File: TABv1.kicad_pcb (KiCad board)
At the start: 4 copper layers, 90 x 45 mm, 120 parts, among them IC1 TPS630702RNMR, J10 Conn_02x03_Odd_Even, J11 Conn_01x06_Pin, J5 Conn_02x08_Odd_Even, J6 Conn_02x08_Odd_Even, J7 503398-1892, J8 1053141104, J9 Conn_02x03_Odd_Even, Q1 MJD44H11T4G, Q10 PJM09P30DF, Q11 PJM09P30DF, Q12 PJM09P30DF, Q2 DMN2040U, Q3 DMN2040U, Q4 BC817-25,215, Q5 DMN2040U, Q6 DMN2040U, Q7 DMN2040U, SW1 BOOTSEL, SW2 RESET, U1 RP2350B-QFN80, U11 LPS22DF, U2 W25Q128JVS, U4 LSM6DSV80XTR, U5 LSM6DSV80XTR, U7 LM334M, U8 LIS2MDL, Y1 12MHz

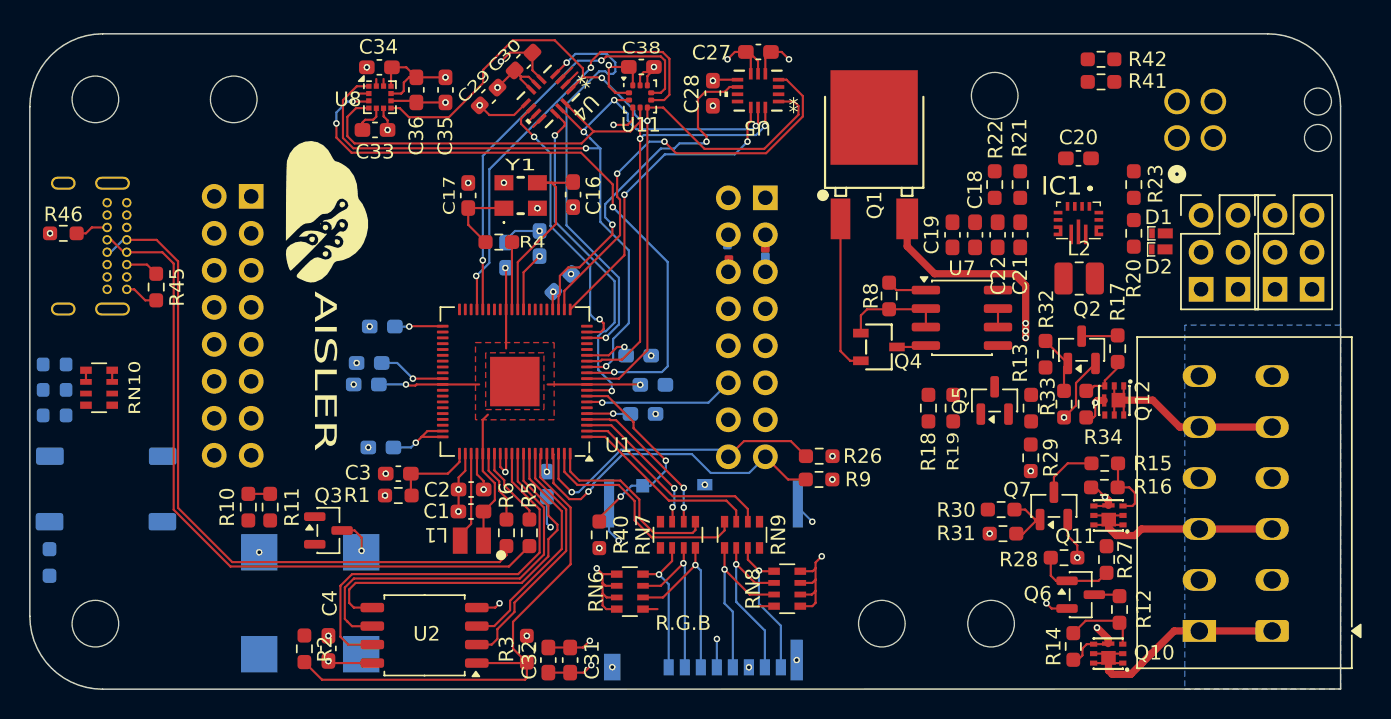
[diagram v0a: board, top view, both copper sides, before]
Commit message: nuovo routing completato (piste 0.15mm)
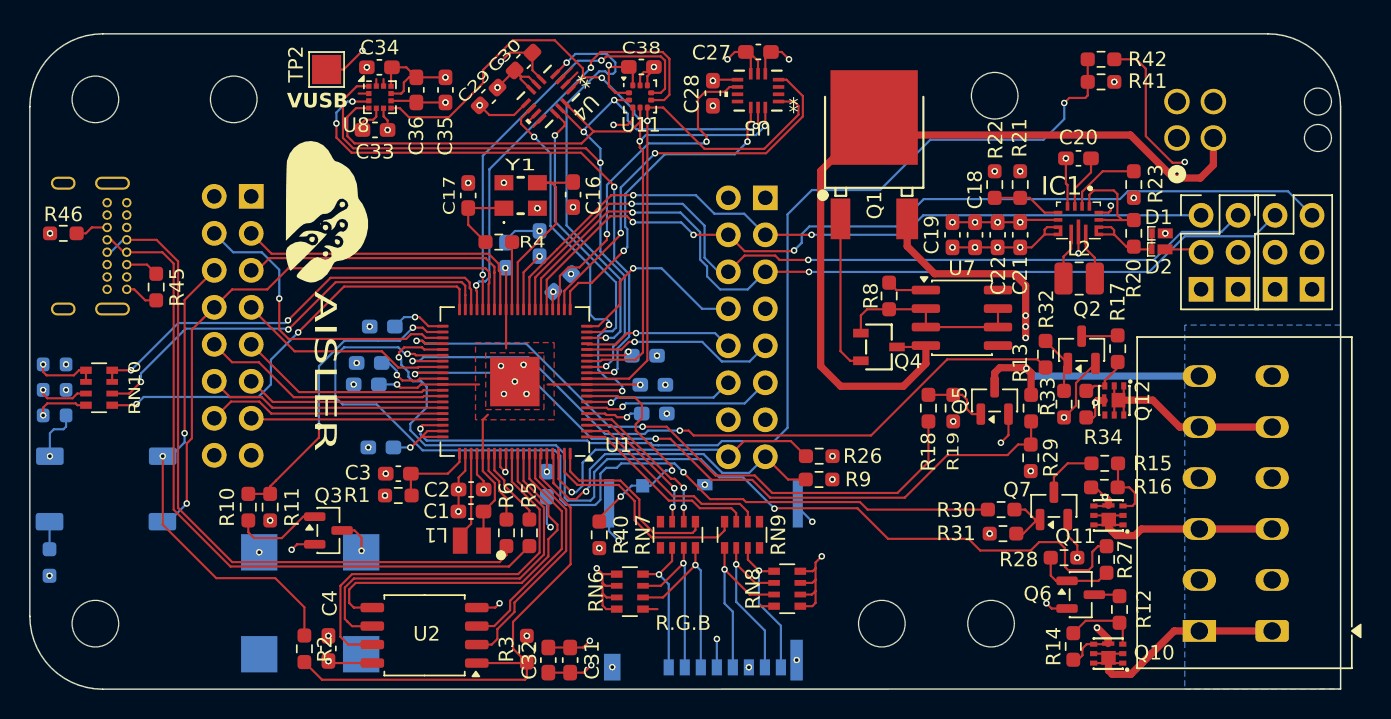
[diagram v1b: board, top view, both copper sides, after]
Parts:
- added TP2: TestPoint, TestPoint:TestPoint_Pad_2.0x2.0mm, F.Cu at (92.9, 36.0)
- moved C5 0.78 mm to (115.4, 59.6)
- moved C12 0.40 mm to (114.7, 55.6)
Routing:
- net /BATT_SENSE: track 0.00 -> 69.9 mm, vias 0 -> 2
- net /PYRO_FIRE_1: track 0.00 -> 69.6 mm, vias 0 -> 2
- net +BATT: track 2.02 -> 70.6 mm, vias 0 -> 1
- net /PYRO_FIRE_2: track 0.00 -> 63.9 mm, vias 0 -> 2
- net /PWM2: track 0.00 -> 60.3 mm, vias 0 -> 2
- net /PWM1: track 0.00 -> 60.2 mm, vias 0 -> 3
- net /PWM3: track 0.00 -> 57.6 mm, vias 0 -> 2
- net /PWM4: track 0.00 -> 52.4 mm, vias 0 -> 2
- net /PYRO_SENSE: track 0.00 -> 50.9 mm, vias 0 -> 2
- net /PYRO_FIRE_3: track 0.00 -> 50.5 mm, vias 0 -> 2
- net /PYRO_ENABLE: track 0.00 -> 45.0 mm, vias 0 -> 2
- net /RESET: track 0.00 -> 39.1 mm, vias 0 -> 1
- net BOOTSEL: track 0.00 -> 33.3 mm, vias 0 -> 2
- net /L_BLUE: track 0.00 -> 29.7 mm, vias 0 -> 2
- net /L_GREEN: track 0.00 -> 29.5 mm, vias 0 -> 2
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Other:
- board text added: "VUSB"

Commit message: USB impeadance matching, silkscreen fix, and routing improvement
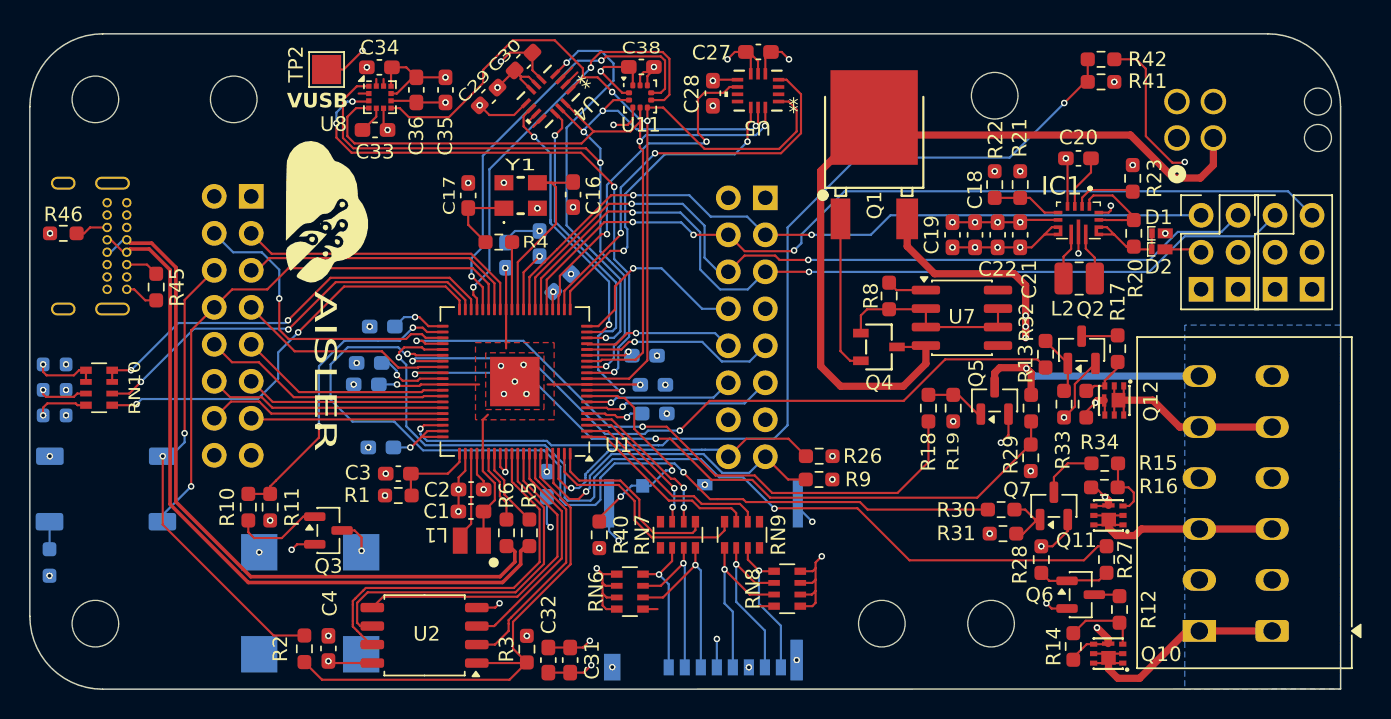
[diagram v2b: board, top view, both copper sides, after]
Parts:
- moved R28 1.57 mm to (141.9, 69.6), turned to -90 degrees
- moved R23 0.43 mm to (148.2, 43.4), turned to -90 degrees
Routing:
- net /PYRO_FIRE_1: track 69.6 -> 65.3 mm
- net GND: track 72.1 -> 68.6 mm, vias 62 -> 63
- net /SD0: track 25.5 -> 22.2 mm
- net /SD3: track 28.1 -> 25.8 mm
- net /BATT_SENSE: track 69.9 -> 68.0 mm
- net /SCLK: track 26.5 -> 24.8 mm
- net D-: track 47.7 -> 49.2 mm
- net D+: track 48.8 -> 50.1 mm
- net BOOTSEL: track 33.3 -> 32.1 mm
- net /L_GREEN: track 29.5 -> 28.6 mm
- net /IMU45_INT1: track 29.6 -> 28.8 mm
- net PG: track 5.13 -> 4.34 mm
- net /SD_detect: track 16.4 -> 15.6 mm
- net /RESET: track 39.1 -> 38.3 mm
- net /SCL_RADIO: track 22.3 -> 21.6 mm
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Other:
- board text removed: "R.G.B"

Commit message: fine rev 2.2
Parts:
- moved H6 2.50 mm to (84.0, 38.0)
- moved H1 0.79 mm to (138.0, 38.0)
- moved H4 0.50 mm to (138.0, 74.0)
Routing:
- net +BATT: track 70.6 -> 71.6 mm
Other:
- board text added: "+"
- board text added: "-"
- board text added: "PPS"
- board text added: "REV 2.2"
- board text added: "RST"
- board text removed: "REV 2.0"

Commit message: Ordine 1 Aprile
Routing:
- net GND: vias 63 -> 104
- added copper zone on B.Cu, net GND
- added copper zone on F.Cu, net GND
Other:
- board text added: "REV 2.3"
- board text removed: "REV 2.2"

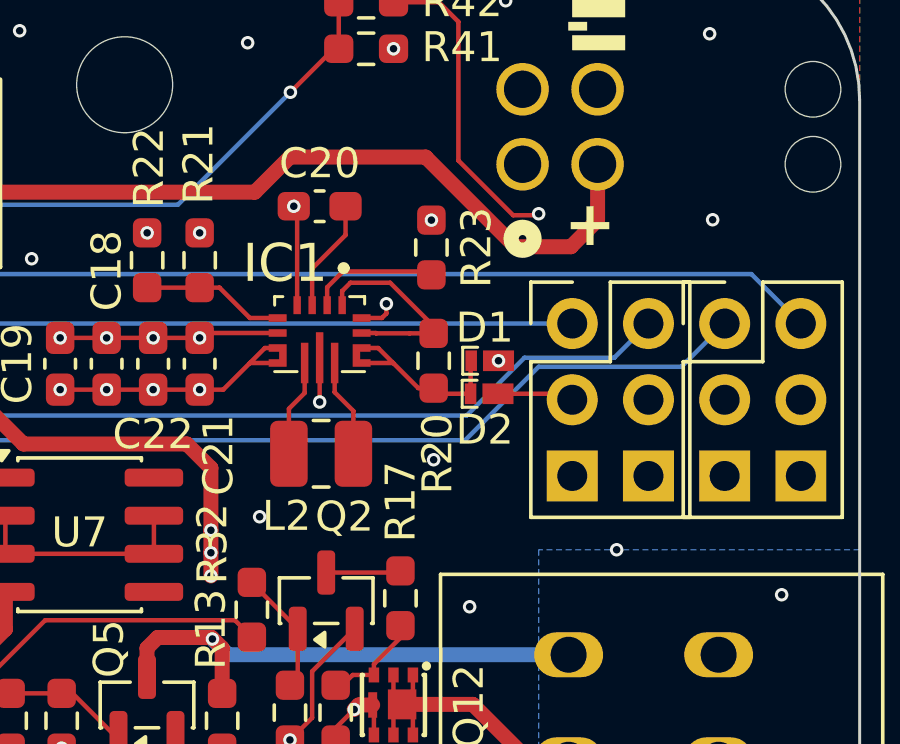
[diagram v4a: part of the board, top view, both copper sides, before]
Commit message: TPS cap added
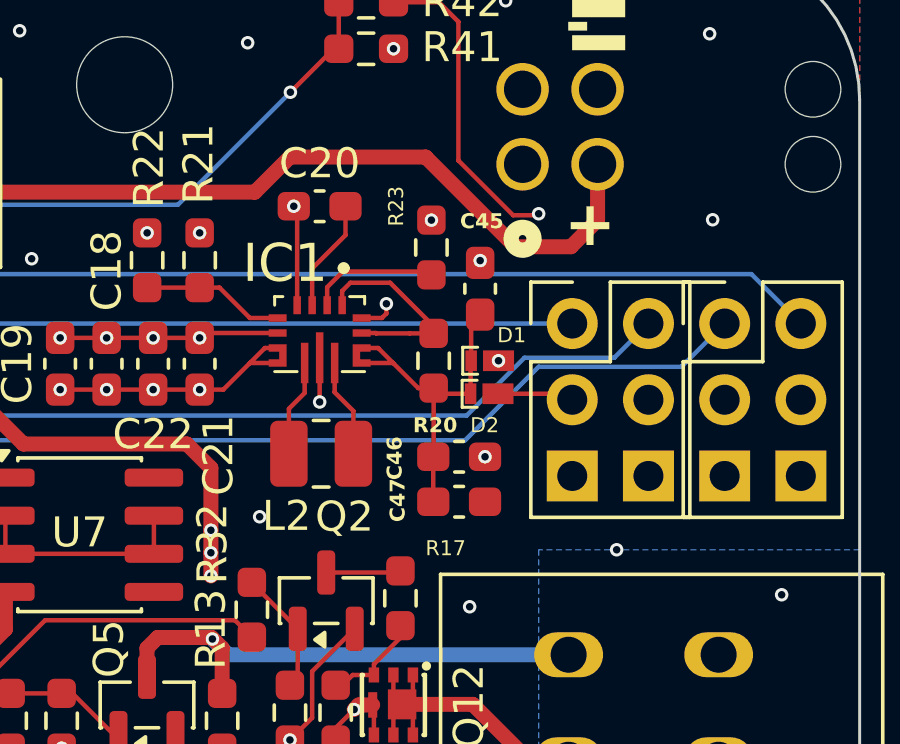
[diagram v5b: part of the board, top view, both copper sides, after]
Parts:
- added C45: 10uF, Capacitor_SMD:C_0603_1608Metric_Pad1.08x0.95mm_HandSolder, F.Cu at (149.8, 44.8)
- added C46: 10uF, Capacitor_SMD:C_0603_1608Metric_Pad1.08x0.95mm_HandSolder, F.Cu at (149.2, 50.4)
- added C47: 10uF, Capacitor_SMD:C_0603_1608Metric_Pad1.08x0.95mm_HandSolder, F.Cu at (149.2, 51.9)
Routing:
- net Net-(D1-K): track 6.42 -> 11.9 mm
- net GND: track 68.6 -> 68.9 mm, vias 104 -> 105
